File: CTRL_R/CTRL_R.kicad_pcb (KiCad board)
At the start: 2 copper layers, 33.4 x 88 mm, 26 parts, among them J1 BM14B-NSHSS-TBT_LF__SN_, J2 BM04B-NSHSS-TBT_LF__SN_, J3 5051100592, U2 74LVC1G08

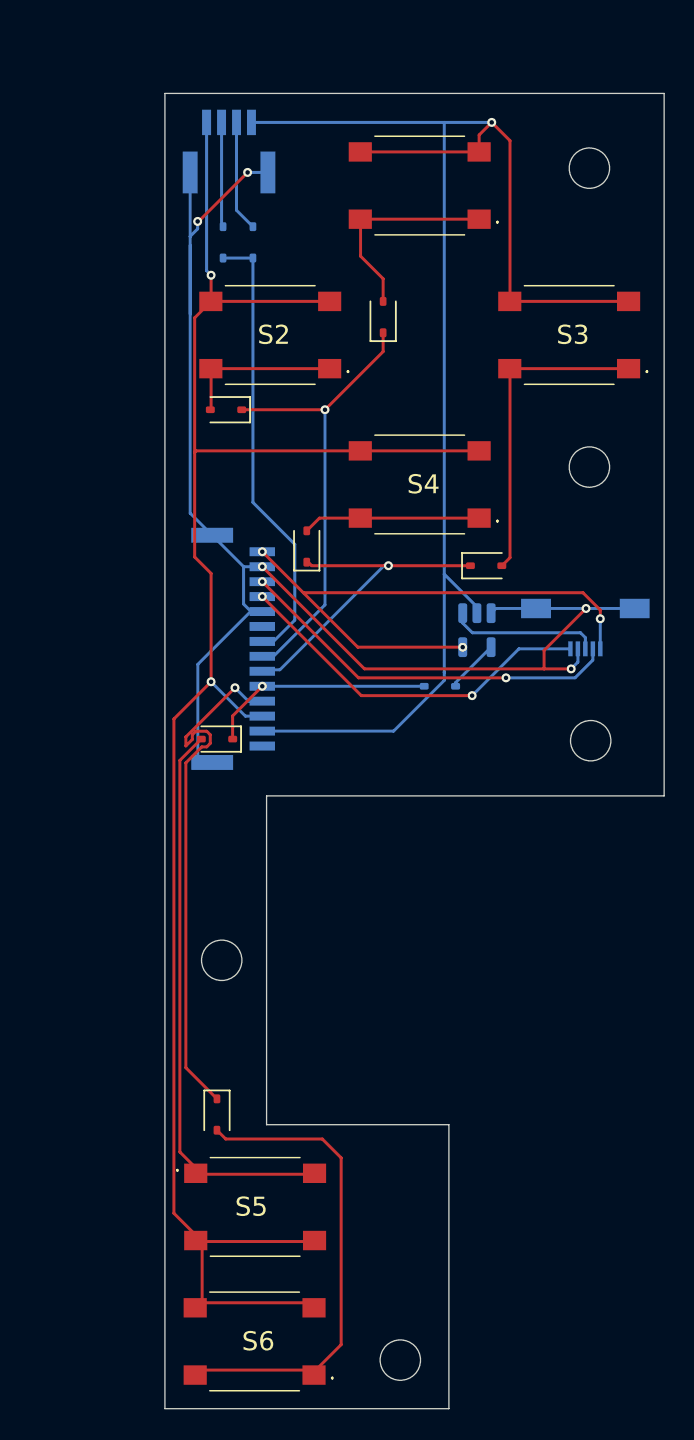
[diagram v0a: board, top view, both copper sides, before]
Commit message: CTRL Z, R, PWR Cleanup! Changes Made:
CTRL PWR -> Added Ground Plane and Ground Vias. Moved it out of parent folder CTRL_R upto Root.
CTRL Z ->  Removed Unnecessary ZX pin. Added Ground Plane and Ground Vias.
CTRL R -> Cleaned up pin count, from 14 down to 10. Added Ground Plane and Ground Vias. Made some modifications to the board shape.
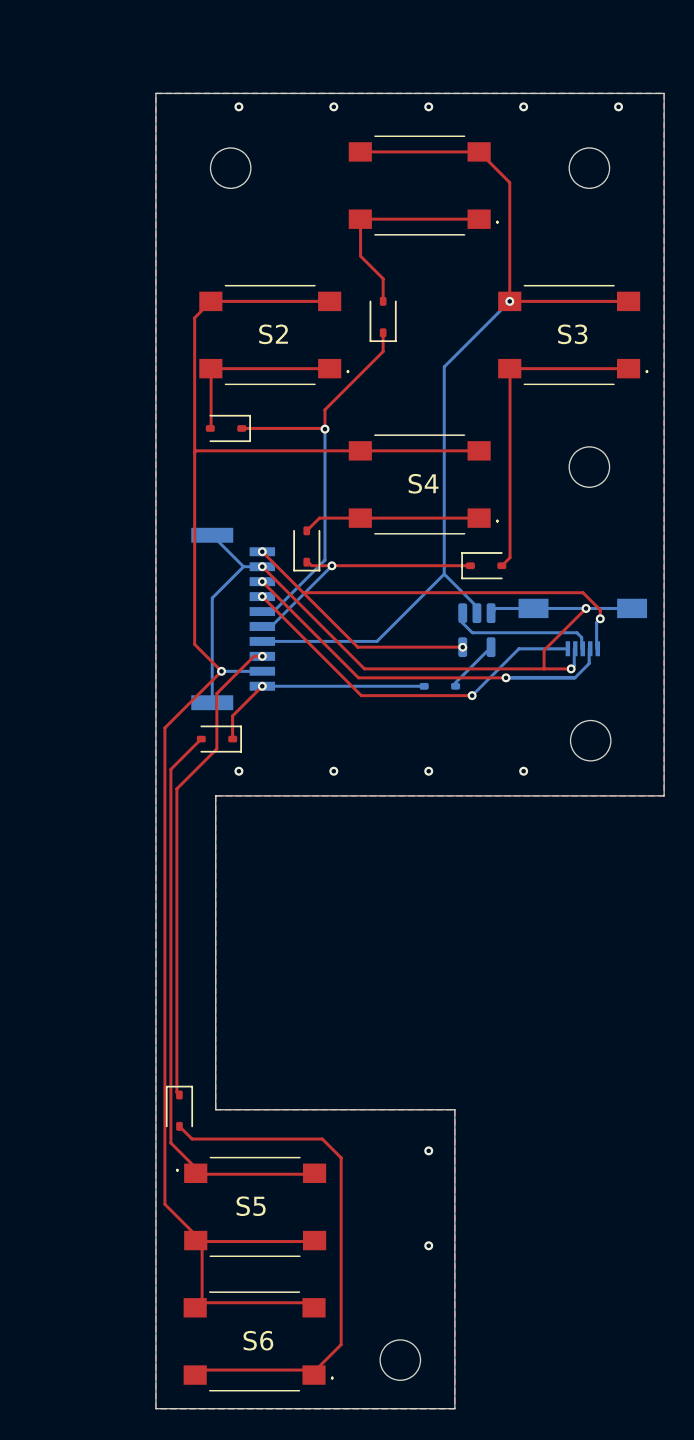
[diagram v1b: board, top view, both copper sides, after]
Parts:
- removed D8, D9: 1N4148WS, Diode_SMD:D_SOD-323
- removed J1: BM14B-NSHSS-TBT_LF__SN_, BM14B-NSHSS-TBT:BM14BNSHSSTBTLFSN
- J2: value BM04B-NSHSS-TBT_LF__SN_ -> BM10B-NSHSS-TBT_LF__SN_; footprint BM04B-NSHSS-TBT:BM04BNSHSSTBTLFSN -> BM10B-NSHSS-TBT_LF__SN_:BM10BNSHSSTBTLFSN
- moved H4 53.0 mm to (82.0, 67.6)
- moved J2 31.0 mm to (81.9, 97.8), turned to 90 degrees
- moved D6 2.52 mm to (78.6, 130.7)
- moved D2 1.25 mm to (81.7, 85.0)
- moved J3 0.17 mm to (105.6, 97.3)
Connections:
- J2 pad 1: Col3 -> +3V3
- J2 pad 2: Net-(D8-A) -> GND
- J2 pad 3: Net-(D9-A) -> /ADC_X
- J2 pad 4: Col4 -> /ADC_Y
- J2 pad 5: GND -> Row2
- J2 pad 6: GND -> Row3
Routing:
- net GND: track 96.9 -> 54.1 mm, vias 5 -> 14
- net Col4: track 101.2 -> 64.0 mm
- net Row1: track 29.4 -> 0.00 mm
- net Col3: track 129.3 -> 116.7 mm, vias 2 -> 1
- net Net-(D9-A): track 7.43 -> 0.00 mm
- net Net-(D8-A): track 6.88 -> 0.00 mm
- net Row3: track 22.3 -> 16.7 mm
- net /ADC_X: track 26.0 -> 30.5 mm
- net Row5: track 35.9 -> 32.1 mm
- net Row2: track 30.3 -> 27.3 mm
- net Net-(D6-A): track 32.1 -> 34.8 mm
- net Net-(D2-A): track 10.7 -> 12.0 mm
- added copper zone on B.Cu, net GND
- added copper zone on F.Cu, net GND
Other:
- board size 33.4 x 88 mm -> 34 x 88 mm

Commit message: Updated CTRL_Z to use 3 pin FPC and ESD Protection.
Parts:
- removed J2: BM10B-NSHSS-TBT_LF__SN_, BM10B-NSHSS-TBT_LF__SN_:BM10BNSHSSTBTLFSN
- added J1: 5034801400, 5034801400:5034801400, B.Cu at (80.2, 97.2)
- added U1: DRV5033FAxDBZ, Package_TO_SOT_SMD:SOT-23, F.Cu at (79.1, 72.1)
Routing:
- net GND: track 54.1 -> 4.95 mm, vias 14 -> 13
- net +3V3: track 39.1 -> 69.9 mm, vias 3 -> 4
- net HALL: track 0.00 -> 21.2 mm, vias 0 -> 1
- net Row4: track 15.2 -> 21.7 mm
- net Row2: track 27.3 -> 33.3 mm
- net Col4: track 64.0 -> 69.9 mm
- net /ADC_X: track 30.5 -> 36.3 mm
- net Row3: track 16.7 -> 22.4 mm
- net /ADC_Y: track 24.4 -> 29.9 mm
- net Col3: track 116.7 -> 113.5 mm

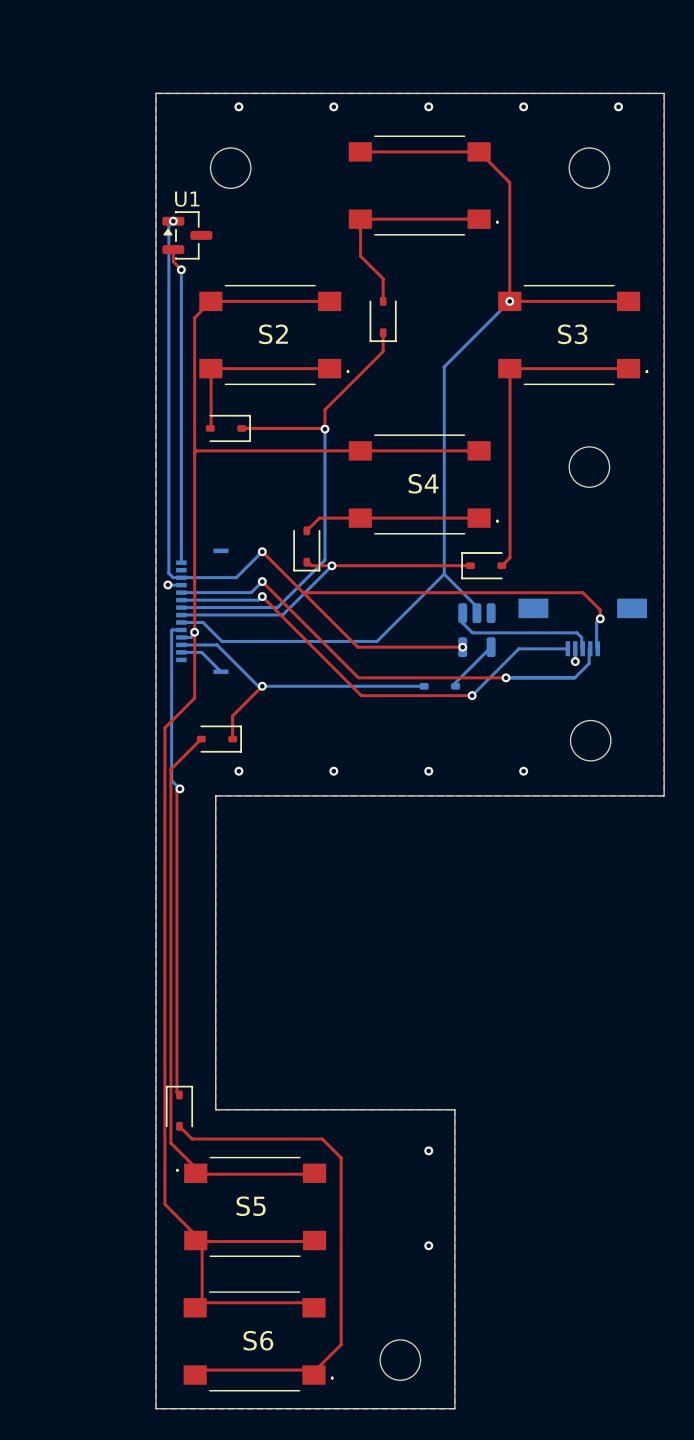
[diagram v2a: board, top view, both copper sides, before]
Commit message: Updated CTRL_R to have ESD diodes, CTRL_Z connector, FPC, yada yada.
Its the same stuff as the commit with CTRL_L.
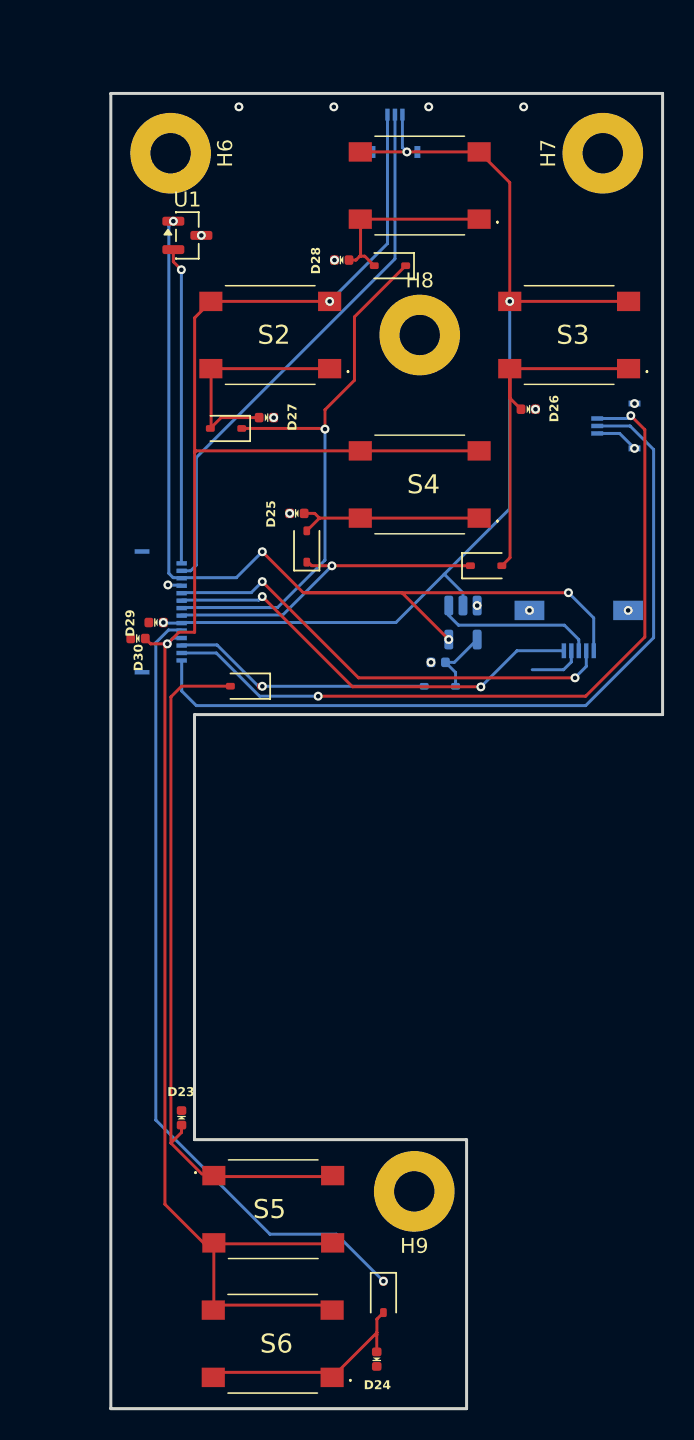
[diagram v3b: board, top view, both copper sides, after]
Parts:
- removed H1, H2, H3, H4, H5: MountingHole, MountingHole:MountingHole_2.7mm_M2.5
- added D23: ESD5V0B03, A_HDJ_Library:D_0402_1005Metric, F.Cu at (78.7, 131.1)
- added D24: ESD5V0B03, A_HDJ_Library:D_0402_1005Metric, F.Cu at (91.8, 147.3)
- added D25: ESD5V0B03, A_HDJ_Library:D_0402_1005Metric, F.Cu at (86.4, 90.7)
- added D26: ESD5V0B03, A_HDJ_Library:D_0402_1005Metric, F.Cu at (101.9, 83.7)
- added D27: ESD5V0B03, A_HDJ_Library:D_0402_1005Metric, F.Cu at (84.4, 84.3)
- added D28: ESD5V0B03, A_HDJ_Library:D_0402_1005Metric, F.Cu at (89.4, 73.8)
- added D29: ESD5V0B03, A_HDJ_Library:D_0402_1005Metric, F.Cu at (77.0, 98.0)
- added D30: ESD5V0B03, A_HDJ_Library:D_0402_1005Metric, F.Cu at (75.8, 99.1)
- added D31: ESD5V0B03, A_HDJ_Library:D_0402_1005Metric, B.Cu at (95.9, 100.7)
- added H6: MountingHole_Pad, MountingHole:MountingHole_2.7mm_M2.5_Pad, F.Cu at (78.0, 66.6)
- added H7: MountingHole_Pad, MountingHole:MountingHole_2.7mm_M2.5_Pad, F.Cu at (106.9, 66.6)
- added H8: MountingHole_Pad, MountingHole:MountingHole_2.7mm_M2.5_Pad, F.Cu at (94.6, 78.8)
- added H9: MountingHole_Pad, MountingHole:MountingHole_2.7mm_M2.5_Pad, F.Cu at (94.3, 136.1)
- added J2: AYF530365TA, AYF530365TA:AYF530365T, B.Cu at (108.0, 84.8)
- added J6: AYF530365TA, AYF530365TA:AYF530365T, B.Cu at (93.0, 65.5)
- moved D6 18.5 mm to (92.2, 143.1)
- moved kibuzzard-6A19F3B7 6.43 mm to (82.7, 148.2), turned to 180 degrees
- moved D5 4.04 mm to (83.0, 102.3)
- moved kibuzzard-6A187131 3.84 mm to (83.4, 143.7), turned to 180 degrees
- moved D1 3.47 mm to (92.7, 74.1), turned to 180 degrees
- moved J1 2.98 mm to (77.2, 97.3), turned to 90 degrees
- moved S5 1.22 mm to (84.8, 137.3)
- moved S6 1.22 mm to (84.8, 146.3)
- moved U2 1.06 mm to (97.5, 98.0)
- moved J3 0.30 mm to (105.3, 97.4)
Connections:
- J1 pad 1: HALL -> SL_BRI
- J1 pad 10: Row5 -> /ADC_X
- J1 pad 11: Col3 -> GND
- J1 pad 12: Row4 -> +3V3
- J1 pad 13: GND -> Row1
- J1 pad 14: SL_BRI -> HALL
- J1 pad 2: Row1 -> SL_VIN
- J1 pad 3: +3V3 -> Row4
- J1 pad 4: GND -> Col3
- J1 pad 5: /ADC_X -> Row5
- J1 pad 6: /ADC_Y -> Col4
- J1 pad 7: Row2 -> Row3
- J1 pad 8: Row3 -> Row2
- J1 pad 9: Col4 -> /ADC_Y
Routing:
- net SL_BRI: track 0.00 -> 52.9 mm
- net SL_VIN: track 0.00 -> 51.4 mm, vias 0 -> 2
- net Row1: track 0.00 -> 36.8 mm
- net Row5: track 32.1 -> 53.7 mm
- net Net-(D24-A2): track 34.8 -> 15.1 mm
- net Col3: track 113.5 -> 131.1 mm, vias 1 -> 2
- net Net-(D23-A2): track 38.8 -> 46.6 mm
- net Row2: track 33.3 -> 38.4 mm
- net /ADC_X: track 36.3 -> 31.4 mm
- net Row4: track 21.7 -> 17.4 mm
- net Net-(D2-A): track 12.0 -> 15.5 mm
- net Net-(D26-A2): track 21.4 -> 24.4 mm
- net GND: track 4.95 -> 7.40 mm, vias 13 -> 16
- net Col4: track 69.9 -> 72.3 mm, vias 1 -> 3
- net +3V3: track 69.9 -> 68.0 mm
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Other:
- board size 34 x 88 mm -> 36.9 x 88 mm

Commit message: Updated CTRL_R to use 4 pin FPC and fixed DRC errors.
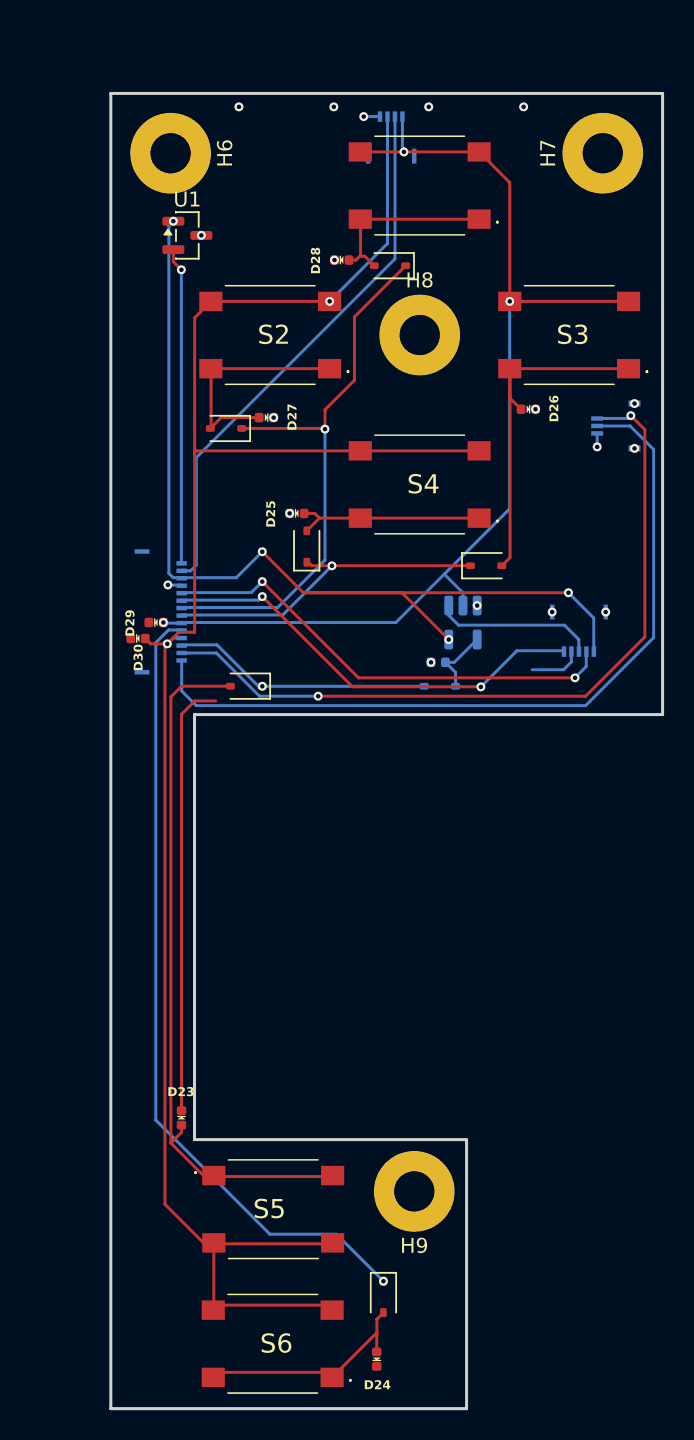
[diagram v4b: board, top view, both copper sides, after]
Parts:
- removed J3: 5051100592, 5051100592:CON_5051100592_MOL
- removed J6: AYF530365TA, AYF530365TA:AYF530365T
- added J4: 503480-0440, 503480-0440:5034800440, B.Cu at (92.7, 65.7)
- added J5: 503480-0540, 503480-0540:5034800540, B.Cu at (105.3, 98.5)
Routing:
- net GND: track 7.40 -> 35.7 mm, vias 16 -> 18

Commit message: Updated CTRLs to be one sided (saves a billion dollars somehow), added LCSC_Parts for BOM, and other fixes. (Part 1/2)
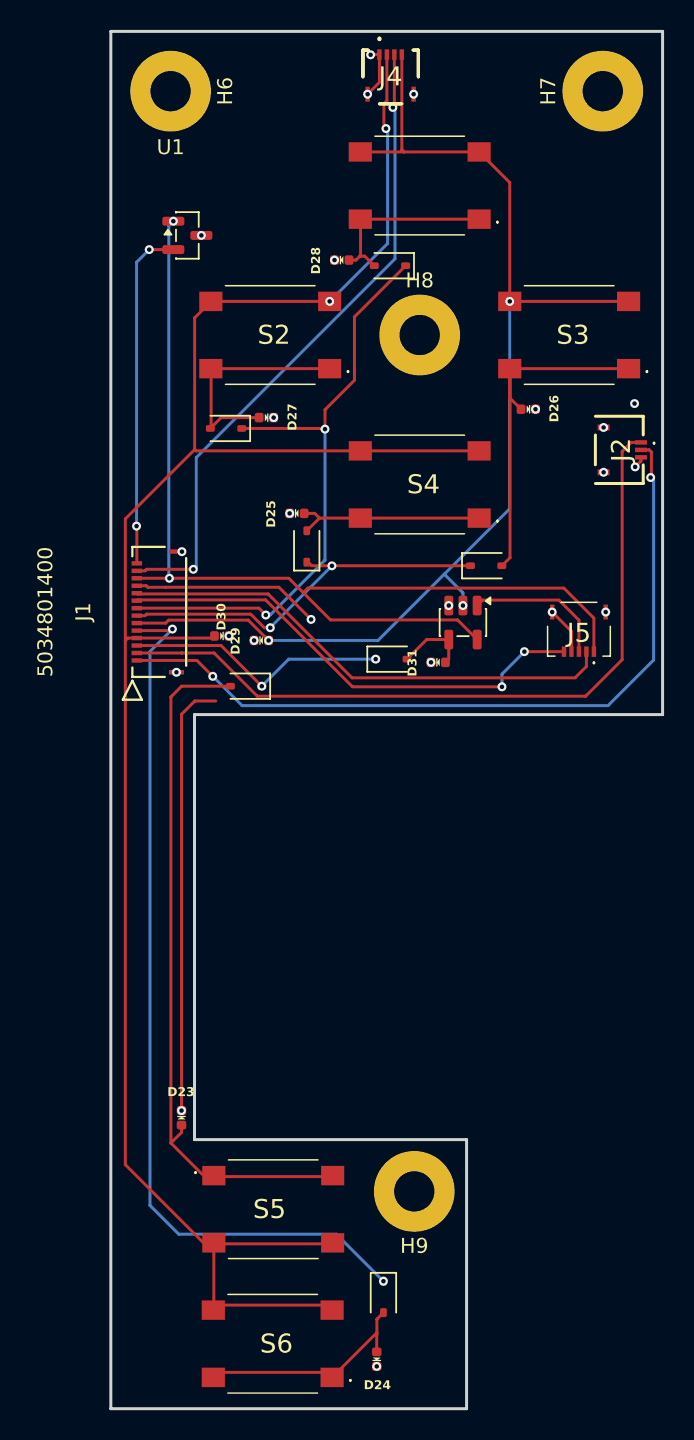
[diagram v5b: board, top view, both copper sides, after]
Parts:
- D31, D7, J1, J2, J4, J5, U2: moved to F.Cu
- moved D29 7.14 mm to (84.0, 99.2)
- moved D30 5.60 mm to (81.4, 98.9), turned to 180 degrees
- moved H7 4.15 mm to (106.9, 62.4)
- moved H6 4.15 mm to (78.0, 62.5)
- moved J4 4.15 mm to (92.7, 61.5), turned to 0 degrees
- moved D7 3.72 mm to (92.8, 100.5)
- moved J2 1.60 mm to (108.0, 86.5)
- turned J5 to 180 degrees
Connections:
- J1 pad 10: /ADC_X -> /ADC_Y
- J1 pad 9: /ADC_Y -> /ADC_X
- J4 pad 1: Col4 -> GND
- J4 pad 2: Row1 -> Col3
- J4 pad 3: Col3 -> Row1
- J4 pad 4: GND -> Col4
- J5 pad 1: /ADC_Y -> +3V3
- J5 pad 2: GND -> /ADC_Y
- J5 pad 4: /ADC_X -> GND
- J5 pad 5: +3V3 -> /ADC_X
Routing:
- net GND: track 35.7 -> 49.7 mm, vias 18 -> 23
- net Col3: track 131.1 -> 140.3 mm
- net Row1: track 36.8 -> 43.9 mm, vias 0 -> 2
- net Col4: track 72.2 -> 79.1 mm
- net Row5: track 53.7 -> 59.3 mm, vias 1 -> 2
- net /ADC_Y: track 29.2 -> 33.7 mm, vias 2 -> 0
- net Row3: track 22.4 -> 26.1 mm, vias 1 -> 2
- net Row2: track 38.4 -> 41.8 mm, vias 1 -> 2
- net +3V3: track 68.0 -> 71.1 mm, vias 4 -> 2
- net HALL: track 21.2 -> 23.0 mm, vias 1 -> 2
- net SL_VIN: track 51.4 -> 50.1 mm, vias 2 -> 0
- net /SW: track 10.8 -> 9.63 mm
- net SL_BRI: track 52.9 -> 51.9 mm, vias 0 -> 2
- net /ADC_X: track 31.4 -> 32.5 mm
- net Row4: track 17.4 -> 17.9 mm, vias 1 -> 2
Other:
- board size 36.9 x 88 mm -> 36.9 x 92.2 mm
